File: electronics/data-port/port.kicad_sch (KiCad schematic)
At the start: 8 parts, among them J1 DATA, J2 LEAD, U1 USBLC6-2SC6

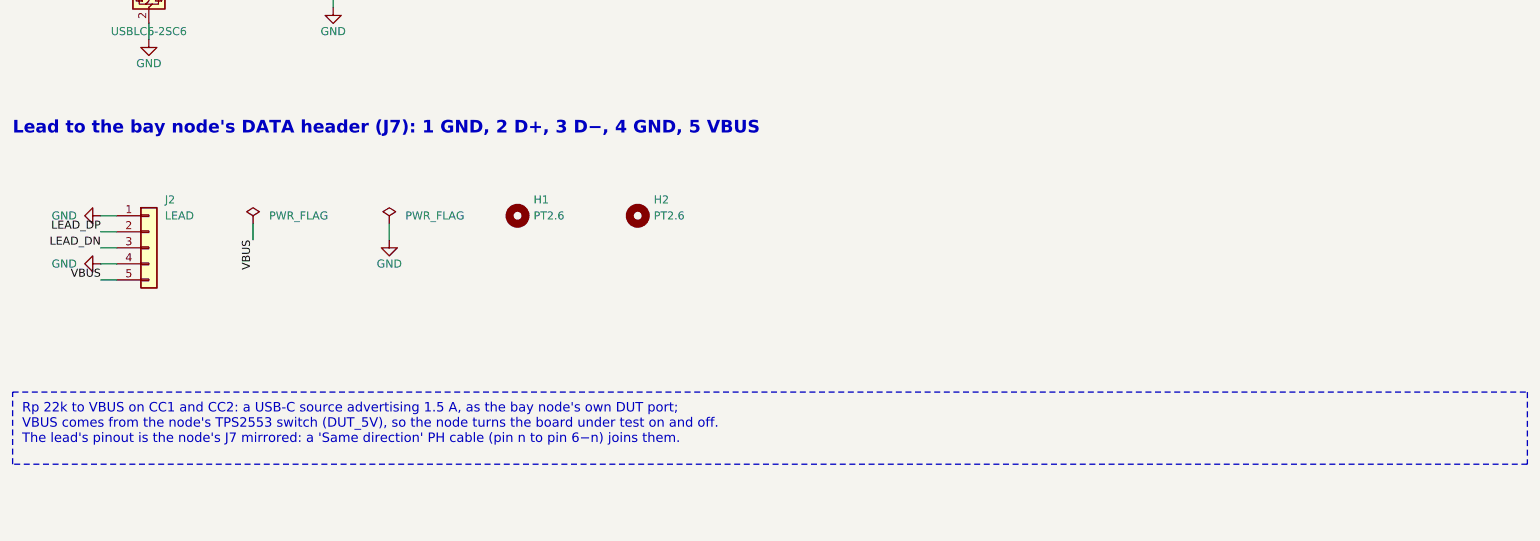
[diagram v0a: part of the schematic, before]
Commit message: DATA lead on 8 wires: node J7 a vertical PH 8 (USB, I²C, INT), data port J2 an S8B
Density decisions of 2026-10-19: the DATA lead becomes the camera's PH 8
"Same direction" type and also carries the node's I²C and an open-drain,
active-low INT (IO4, 10k pull-up, 1k at J7) for a later DATA ×4 board.

- Node: J7 B8B vertical by the right edge (J5's old slot), J5 AUX
  horizontal in the middle, AUX parts in a column between them.  J7 now
  taps the pair at J4's pads (DUT_CONN_*, behind U8's ESD like J4); the
  branch is hand-drawn in usb_hs_routes() on B.Cu under J4, since
  Freerouting found no room on U8's mux side.  ERC 0, DRC 0, parity 0,
  99 models.
- Data port: S8B, pins 1–3 open, PH at x 14.4, left hole (2.6, 13.5),
  one silkscreen label per pin.  ERC 0, DRC 0, parity 0.
- Pin map (README, check_pinmap: DATA_INT reserved), docs, cabling,
  BOM (one PH 8 lead type for DATA and camera, no B5B/S5B), SCAD config.

Co-Authored-By: Claude Opus 5.5 <noreply@anthropic.com>
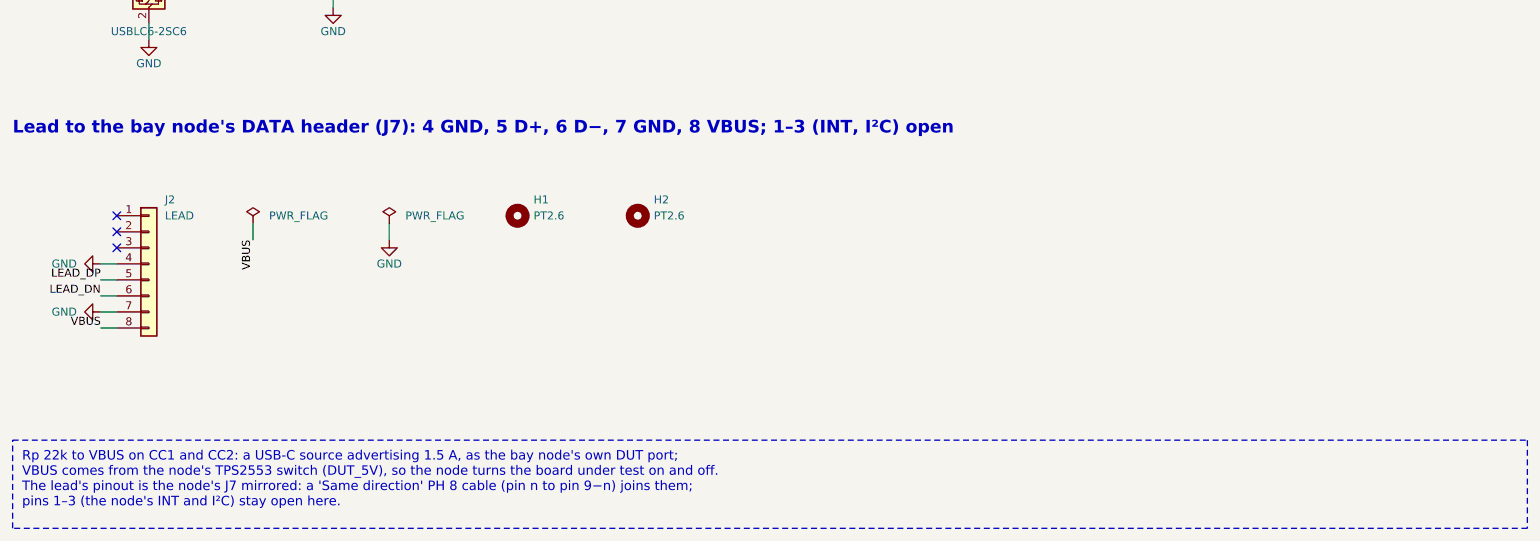
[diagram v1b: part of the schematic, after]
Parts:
- J2: footprint Connector_JST:JST_PH_S5B-PH-SM4-TB_1x05-1MP_P2.00mm_Horizontal -> Connector_JST:JST_PH_S8B-PH-SM4-TB_1x08-1MP_P2.00mm_Horizontal; symbol Connector_Generic:Conn_01x05 -> Connector_Generic:Conn_01x08; LCSC C265104 -> C265121; MPN S5B-PH-SM4-TB(LF)(SN) -> S8B-PH-SM4-TB(LF)(SN)
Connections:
- net GND: now also J2.7 (Pin_7); no longer J2.1 (Pin_1)
- net LEAD_DN: now also J2.6 (Pin_6); no longer J2.3 (Pin_3)
- net LEAD_DP: now also J2.5 (Pin_5); no longer J2.2 (Pin_2)
- net VBUS: now also J2.8 (Pin_8); no longer J2.5 (Pin_5)
- no-connect marks 2 -> 5
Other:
- note added: "Lead to the bay node's DATA header (J7): 4 GND, 5 D+, 6 D−, 7 GND, 8 VBUS; 1–3 (INT, I²C) open"
- note removed: "Lead to the bay node's DATA header (J7): 1 GND, 2 D+, 3 D−, 4 GND, 5 VBUS"
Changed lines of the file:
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@@
 		)
 	)
-	(text "Lead to the bay node's DATA header (J7): 1 GND, 2 D+, 3 D−, 4 GND, 5 VBUS"
+	(text "Lead to the bay node's DATA header (J7): 4 GND, 5 D+, 6 D−, 7 GND, 8 VBUS; 1–3 (INT, I²C) open"
 		(exclude_from_sim no)
 		(at 20.32 149.86 0)
@@
 	)
 	(symbol
-		(lib_id "Connector_Generic:Conn_01x05")
-		(at 41.91 167.64 0)
+		(lib_id "Connector_Generic:Conn_01x08")
+		(at 41.91 170.18 0)
 		(unit 1)
 		(exclude_from_sim no)
@@
 			)
 		)
-		(property "Footprint" "Connector_JST:JST_PH_S5B-PH-SM4-TB_1x05-1MP_P2.00mm_Horizontal"
-			(at 41.91 167.64 0)
+		(property "Footprint" "Connector_JST:JST_PH_S8B-PH-SM4-TB_1x08-1MP_P2.00mm_Horizontal"
+			(at 41.91 170.18 0)
 			(effects
 				(font
@@
 		)
 		(property "Datasheet" ""
-			(at 41.91 167.64 0)
-			(effects
-				(font
-					(size 1.27 1.27)
-				)
-				(hide yes)
-			)
-		)
-		(property "Description" "JST PH 5-pin, side entry, SMD"
-			(at 41.91 167.64 0)
-			(effects
-				(font
-					(size 1.27 1.27)
-				)
-				(hide yes)
-			)
-		)
-		(property "MPN" "S5B-PH-SM4-TB(LF)(SN)"
-			(at 41.91 167.64 0)
+			(at 41.91 170.18 0)
+			(effects
+				(font
+					(size 1.27 1.27)
+				)
+				(hide yes)
+			)
+		)
+		(property "Description" "JST PH 8-pin, side entry, SMD"
+			(at 41.91 170.18 0)
+			(effects
+				(font
+					(size 1.27 1.27)
+				)
+				(hide yes)
+			)
+		)
+		(property "MPN" "S8B-PH-SM4-TB(LF)(SN)"
+			(at 41.91 170.18 0)
 			(effects
 				(font
@@
 		)
 		(property "Manufacturer" "JST"
-			(at 41.91 167.64 0)
-			(effects
-				(font
-					(size 1.27 1.27)
-				)
-				(hide yes)
-			)
-		)
-		(property "LCSC" "C265104"
-			(at 41.91 167.64 0)
+			(at 41.91 170.18 0)
+			(effects
+				(font
+					(size 1.27 1.27)
+				)
+				(hide yes)
+			)
+		)
+		(property "LCSC" "C265121"
+			(at 41.91 170.18 0)
 			(effects
 				(font
@@
 		)
 		(pin "5"
+		)
+		(pin "6"
+		)
+		(pin "7"
+		)
+		(pin "8"
 		)
 		(instances
@@
 		)
 	)
-	(wire
-		(pts
-			(xy 36.83 162.56)
-			(xy 34.29 162.56)
-		)
-		(stroke
-			(width 0)
-			(type default)
-		)
-	)
-	(symbol
-		(lib_id "power:GND")
-		(at 34.29 162.56 270)
-		(unit 1)
-		(exclude_from_sim no)
-		(in_bom yes)
-		(on_board yes)
-		(dnp no)
-		(fields_autoplaced yes)
-		(property "Reference" "#PWR02005"
-			(at 34.29 162.56 0)
-			(effects
-				(font
-					(size 1.27 1.27)
-				)
-				(hide yes)
-			)
-		)
-		(property "Value" "GND"
-			(at 28.5 162.56 90)
-			(effects
-				(font
-					(size 1.27 1.27)
-				)
-			)
-		)
-		(property "Footprint" ""
-			(at 34.29 162.56 0)
-			(effects
-				(font
-					(size 1.27 1.27)
-				)
-				(hide yes)
-			)
-		)
-		(property "Datasheet" ""
-			(at 34.29 162.56 0)
-			(effects
-				(font
-					(size 1.27 1.27)
-				)
-				(hide yes)
-			)
-		)
-		(property "Description" ""
-			(at 34.29 162.56 0)
-			(effects
-				(font
-					(size 1.27 1.27)
-				)
-				(hide yes)
-			)
-		)
-		(pin "1"
-		)
-		(instances
-			(project "data-port"
-				(path "/4a677053-8451-5b26-9400-50c098a33d8f/351729e2-850e-559f-aa34-46144b490769"
-					(reference "#PWR02005")
-					(unit 1)
-				)
-			)
-		)
-	)
-	(wire
-		(pts
-			(xy 36.83 165.1)
-			(xy 34.29 165.1)
-		)
-		(stroke
-			(width 0)
-			(type default)
-		)
-	)
-	(label "LEAD_DP"
-		(at 34.29 165.1 180)
-		(fields_autoplaced yes)
-		(effects
-			(font
-				(size 1.27 1.27)
-			)
-			(justify right bottom)
-		)
-	)
-	(wire
-		(pts
-			(xy 36.83 167.64)
-			(xy 34.29 167.64)
-		)
-		(stroke
-			(width 0)
-			(type default)
-		)
-	)
-	(label "LEAD_DN"
-		(at 34.29 167.64 180)
-		(fields_autoplaced yes)
-		(effects
-			(font
-				(size 1.27 1.27)
-			)
-			(justify right bottom)
-		)
+	(no_connect
+		(at 36.83 162.56)
+	)
+	(no_connect
+		(at 36.83 165.1)
+	)
+	(no_connect
+		(at 36.83 167.64)
 	)
 	(wire
@@
 		(dnp no)
 		(fields_autoplaced yes)
-		(property "Reference" "#PWR02006"
+		(property "Reference" "#PWR02005"
 			(at 34.29 170.18 0)
 			(effects
@@
 		(property "Description" ""
 			(at 34.29 170.18 0)
+			(effects
+				(font
+					(size 1.27 1.27)
+				)
+				(hide yes)
+			)
+		)
+		(pin "1"
+		)
+		(instances
+			(project "data-port"
+				(path "/4a677053-8451-5b26-9400-50c098a33d8f/351729e2-850e-559f-aa34-46144b490769"
+					(reference "#PWR02005")
+					(unit 1)
+				)
+			)
+		)
+	)
+	(wire
+		(pts
+			(xy 36.83 172.72)
+			(xy 34.29 172.72)
+		)
+		(stroke
+			(width 0)
+			(type default)
+		)
+	)
+	(label "LEAD_DP"
+		(at 34.29 172.72 180)
+		(fields_autoplaced yes)
+		(effects
+			(font
+				(size 1.27 1.27)
+			)
+			(justify right bottom)
+		)
+	)
+	(wire
+		(pts
+			(xy 36.83 175.26)
+			(xy 34.29 175.26)
+		)
+		(stroke
+			(width 0)
+			(type default)
+		)
+	)
+	(label "LEAD_DN"
+		(at 34.29 175.26 180)
+		(fields_autoplaced yes)
+		(effects
+			(font
+				(size 1.27 1.27)
+			)
+			(justify right bottom)
+		)
+	)
+	(wire
+		(pts
+			(xy 36.83 177.8)
+			(xy 34.29 177.8)
+		)
+		(stroke
+			(width 0)
+			(type default)
+		)
+	)
+	(symbol
+		(lib_id "power:GND")
+		(at 34.29 177.8 270)
+		(unit 1)
+		(exclude_from_sim no)
+		(in_bom yes)
+		(on_board yes)
+		(dnp no)
+		(fields_autoplaced yes)
+		(property "Reference" "#PWR02006"
+			(at 34.29 177.8 0)
+			(effects
+				(font
+					(size 1.27 1.27)
+				)
+				(hide yes)
+			)
+		)
+		(property "Value" "GND"
+			(at 28.5 177.8 90)
+			(effects
+				(font
+					(size 1.27 1.27)
+				)
+			)
+		)
+		(property "Footprint" ""
+			(at 34.29 177.8 0)
+			(effects
+				(font
+					(size 1.27 1.27)
+				)
+				(hide yes)
+			)
+		)
+		(property "Datasheet" ""
+			(at 34.29 177.8 0)
+			(effects
+				(font
+					(size 1.27 1.27)
+				)
+				(hide yes)
+			)
+		)
+		(property "Description" ""
+			(at 34.29 177.8 0)
 			(effects
 				(font
@@
 	(wire
 		(pts
-			(xy 36.83 172.72)
-			(xy 34.29 172.72)
+			(xy 36.83 180.34)
+			(xy 34.29 180.34)
 		)
 		(stroke
@@
 	)
 	(label "VBUS"
-		(at 34.29 172.72 180)
+		(at 34.29 180.34 180)
 		(fields_autoplaced yes)
 		(effects
@@
 		)
 	)
-	(text_box "Rp 22k to VBUS on CC1 and CC2: a USB-C source advertising 1.5 A, as the bay node's own DUT port;\n  VBUS comes from the node's TPS2553 switch (DUT_5V), so the node turns the board under test on and off.\nThe lead's pinout is the node's J7 mirrored: a 'Same direction' PH cable (pin n to pin 6−n) joins them."
+	(text_box "Rp 22k to VBUS on CC1 and CC2: a USB-C source advertising 1.5 A, as the bay node's own DUT port;\n  VBUS comes from the node's TPS2553 switch (DUT_5V), so the node turns the board under test on and off.\nThe lead's pinout is the node's J7 mirrored: a 'Same direction' PH 8 cable (pin n to pin 9−n) joins them;\n  pins 1–3 (the node's INT and I²C) stay open here."
 		(exclude_from_sim no)
-		(at 20.32 190.5 0)
-		(size 240.03 11.43)
+		(at 20.32 198.12 0)
+		(size 240.03 13.97)
 		(margins 1.5 1.5 1.5 1.5)
 		(stroke

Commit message: Bay node: J7 takes D+ on pin 3, the DUT pair runs straight
U8 puts D- to the north and J7's side entry put D+ there, so D+ crossed
under D- on B.Cu.  The user chose to swap J7's pins 3/4 (3 D+, 4 D-):
DUT_CONN_DP/DN now run straight from U8 into J7, one 45° step each, no
via (14.6 / 14.7 mm; J3 -> J7 matched to ≈ 0.3 mm).

The data port follows through the lead (pin n <-> 9-n): J2 5 D-, 6 D+,
and U1's channels swap with it (D+ through 1/6), so every pad keeps the
copper it had.  Both boards re-routed: ERC 0, DRC 0, 0 unconnected,
parity 0, JLC READY.

The node's buck GND and +5V islands and the LDO tab are now exclusive
(0.5 mm), as on the hub: Freerouting cut buck-5v, then C12 off the LDO
tab.  Docs: electronics (HS path, J7 and lead pinouts), cabling, the
third Konnect round; BOM note.

Co-Authored-By: Claude Opus 5.5 <noreply@anthropic.com>
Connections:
- net CONN_DN: now also U1.4 (I/O2); no longer U1.6 (I/O1)
- net CONN_DP: now also U1.6 (I/O1); no longer U1.4 (I/O2)
- net LEAD_DN: now also J2.5 (Pin_5), U1.3 (I/O2); no longer J2.6 (Pin_6), U1.1 (I/O1)
- net LEAD_DP: now also J2.6 (Pin_6), U1.1 (I/O1); no longer J2.5 (Pin_5), U1.3 (I/O2)
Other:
- note added: "Lead to the bay node's DATA header (J7): 4 GND, 5 D−, 6 D+, 7 GND, 8 VBUS; 1–3 (INT, I²C) open"
- note removed: "Lead to the bay node's DATA header (J7): 4 GND, 5 D+, 6 D−, 7 GND, 8 VBUS; 1–3 (INT, I²C) open"
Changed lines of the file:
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@@
 		)
 	)
-	(text "Lead to the bay node's DATA header (J7): 4 GND, 5 D+, 6 D−, 7 GND, 8 VBUS; 1–3 (INT, I²C) open"
+	(text "Lead to the bay node's DATA header (J7): 4 GND, 5 D−, 6 D+, 7 GND, 8 VBUS; 1–3 (INT, I²C) open"
 		(exclude_from_sim no)
 		(at 20.32 149.86 0)
@@
 		)
 	)
-	(label "LEAD_DN"
+	(label "LEAD_DP"
 		(at 34.29 124.46 180)
 		(fields_autoplaced yes)
@@
 		)
 	)
-	(label "LEAD_DP"
+	(label "LEAD_DN"
 		(at 34.29 127 180)
 		(fields_autoplaced yes)
@@
 		)
 	)
-	(label "CONN_DP"
+	(label "CONN_DN"
 		(at 49.53 127 0)
 		(fields_autoplaced yes)
@@
 		)
 	)
-	(label "CONN_DN"
+	(label "CONN_DP"
 		(at 49.53 124.46 0)
 		(fields_autoplaced yes)
@@
 		)
 	)
-	(label "LEAD_DP"
+	(label "LEAD_DN"
 		(at 34.29 172.72 180)
 		(fields_autoplaced yes)
@@
 		)
 	)
-	(label "LEAD_DN"
+	(label "LEAD_DP"
 		(at 34.29 175.26 180)
 		(fields_autoplaced yes)

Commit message: DATA port: the PCBA review's fixes
D1: VBUS drawn, 0.8 mm F.Cu from J2.8 under the PH's housing into both of
J1's VBUS pad pairs, necked to 0.5 mm at the pad row (about 15 mOhm
instead of the routed 0.25 mm's 0.13 Ohm), in a Power netclass; thin
tracks to the Rp, C1 and the ESD's VBUS pin.  D2: 10 uF 0805 at the
receptacle (C2, a basic part).  D3: Rp 56k, "default USB power" as on
the DATA x4: 22k would advertise 1.5 A, above the node's TPS2553D low
end of 1.34 A.  D4: a meter check of each PH 8 lead in assembly.md.  D5:
checked in SolidCraft on B-rep (port wall with its U, board, USB4105, a
largest-size plug overmold): the mouth's 0.28 mm overhang sits inside
the U, 2.2 mm clear each side; the overmold clears it by 0.2 mm.

The CPL audit agrees on all 7 parts.  ERC 0, DRC 0, parity 0, 0
unconnected; the BOM follows.

Co-Authored-By: Claude Opus 5.5 <noreply@anthropic.com>
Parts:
- added C2: 10u, Capacitor_SMD:C_0805_2012Metric, symbol Device:C
- R1, R2: value 22k -> 56k; LCSC C31850 -> C23206; MPN 0603WAF2202T5E -> 0603WAF5602T5E
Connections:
- net GND: now also C2.2
- net VBUS: now also C2.1
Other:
- note added: "USB-C receptacle (source): Rp 56k on each CC, the shell to GND, 10 µF on VBUS"
- note removed: "USB-C receptacle (source): Rp 22k on each CC, the shell to GND"

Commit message: Boards: labelled bottom test pads; hub dVdT 100 nF, 50 ms FLT blank
Eve's DFT rule on the four boards this session owns: bare pads on the
bottom, named on B.SilkS, out of the BOM and the CPL (no part, no
assembly fee).  Supply pads 1.5 mm, signal pads 1.0 mm (new catalog
entry "testpad1"), all more than 2 mm from any THT pad or hole
(closest: 4.7 mm, the pod's TP4).  Positions are fixed in design.py,
so they stay put across revisions.

- bay node, 17: TX, RX, 3V3, GND by the module (kept), then EN, IO0,
  FLT (DUT_FLT_N), ALRT (INA_ALERT_N), SDA, SCL and a second GND;
  a supply row along the bottom edge: GND, VIN, 5V, 3V3, DUT 5V,
  CAM 5V
- power hub, 20: TX, RX, 3V3, GND, 5V, VRACK, GND (kept), then EN,
  IO0, the CH224A's PD SDA/SCL, each row's FLT and IMON (A-D) and a
  third GND in the middle
- camera pod, 4: GND, 5V, 3V3 and a second GND at the far end
- DATA port, 2: GND and 5V (VBUS, through a via under its track)

Hub, as the datasheet audit's U1 answer asks (TPS2660 Fig. 55 at
85 C: 8-10 ms at 21 W fails the 47 nF worst start, 33 ms at 14 W
covers 100 nF): C21-C24 dVdT 47 nF -> 100 nF, so a row's soft start
is 16-22 ms and dissipates about 7-9 W typical, 14 W worst, for
19-24 ms; the firmware's HUB_ROW_FLT_BLANK_MS goes 25 -> 50 ms to
cover it (worst case 39 ms).  docs/power.md, the audit row and the
hub notes say so.

Routing fallout: J1's A12/B1 GND now leaves through one drawn 0.5 mm
via so the automatic fan-out can't cut the VRACK pour off A9/B4; the
pod's LDO tab zones are exclusive so tracks no longer split them.

All four rerouted, tidied and checked: ERC 0, DRC 0, unconnected 0,
parity 0.  Gerbers, renders, schematics, viewer GLBs, the JLC
snapshot lines and the rack BOM regenerated.

Co-Authored-By: Claude Opus 5.5 <noreply@anthropic.com>
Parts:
- added TP1: GND, TestPoint:TestPoint_Pad_D1.5mm, symbol Connector:TestPoint
- added TP2: VBUS, TestPoint:TestPoint_Pad_D1.5mm, symbol Connector:TestPoint
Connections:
- net GND: now also TP1.1
- net VBUS: now also TP2.1
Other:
- note added: "Test pads (bottom side, labelled): no short to GND, then VBUS at power-up"
